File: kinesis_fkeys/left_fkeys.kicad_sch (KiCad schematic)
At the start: 20 parts, among them J2 LEFT_13_TOP, J3 Conn_01x08

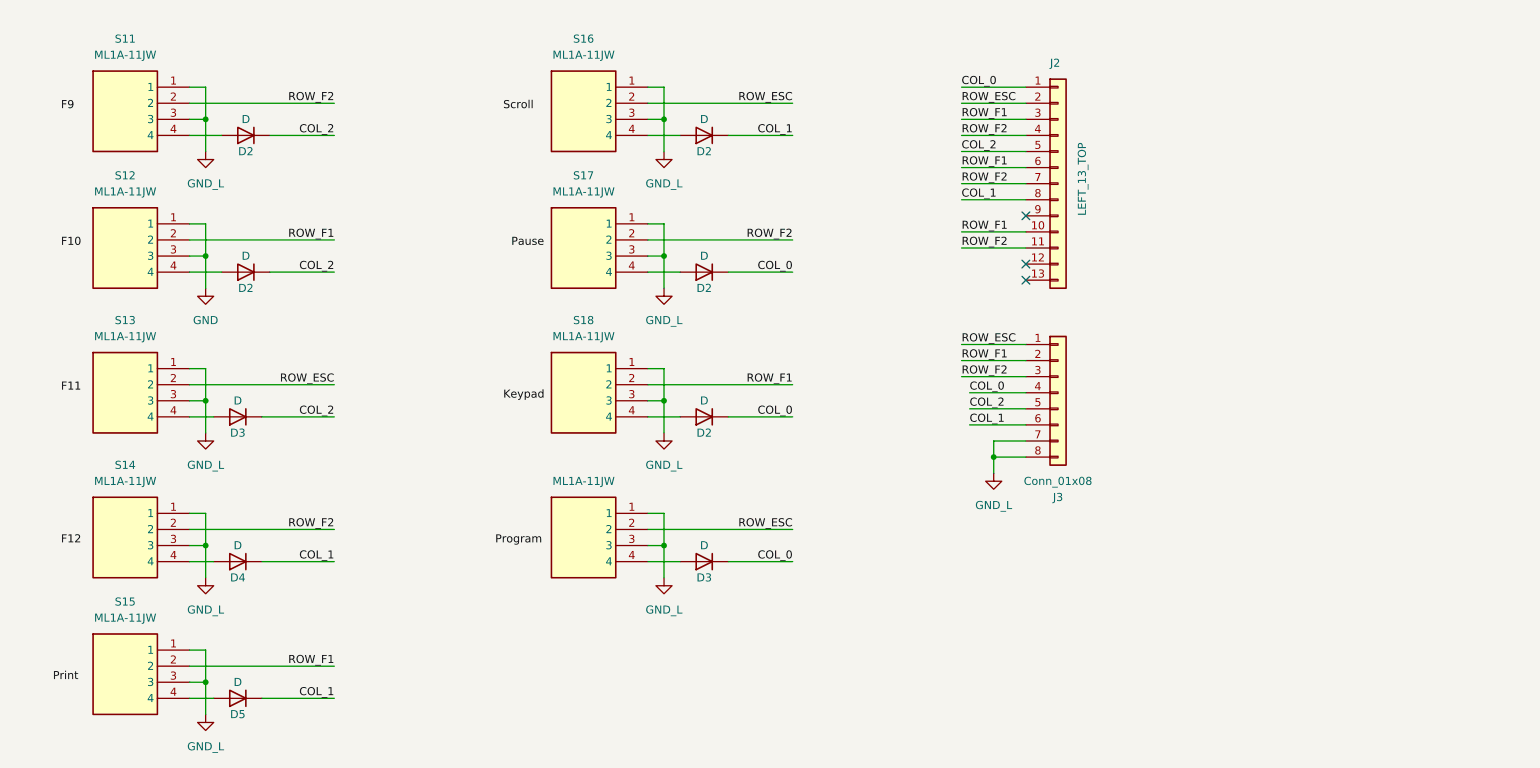
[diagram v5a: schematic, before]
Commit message: created layout - needs to be modified a bit
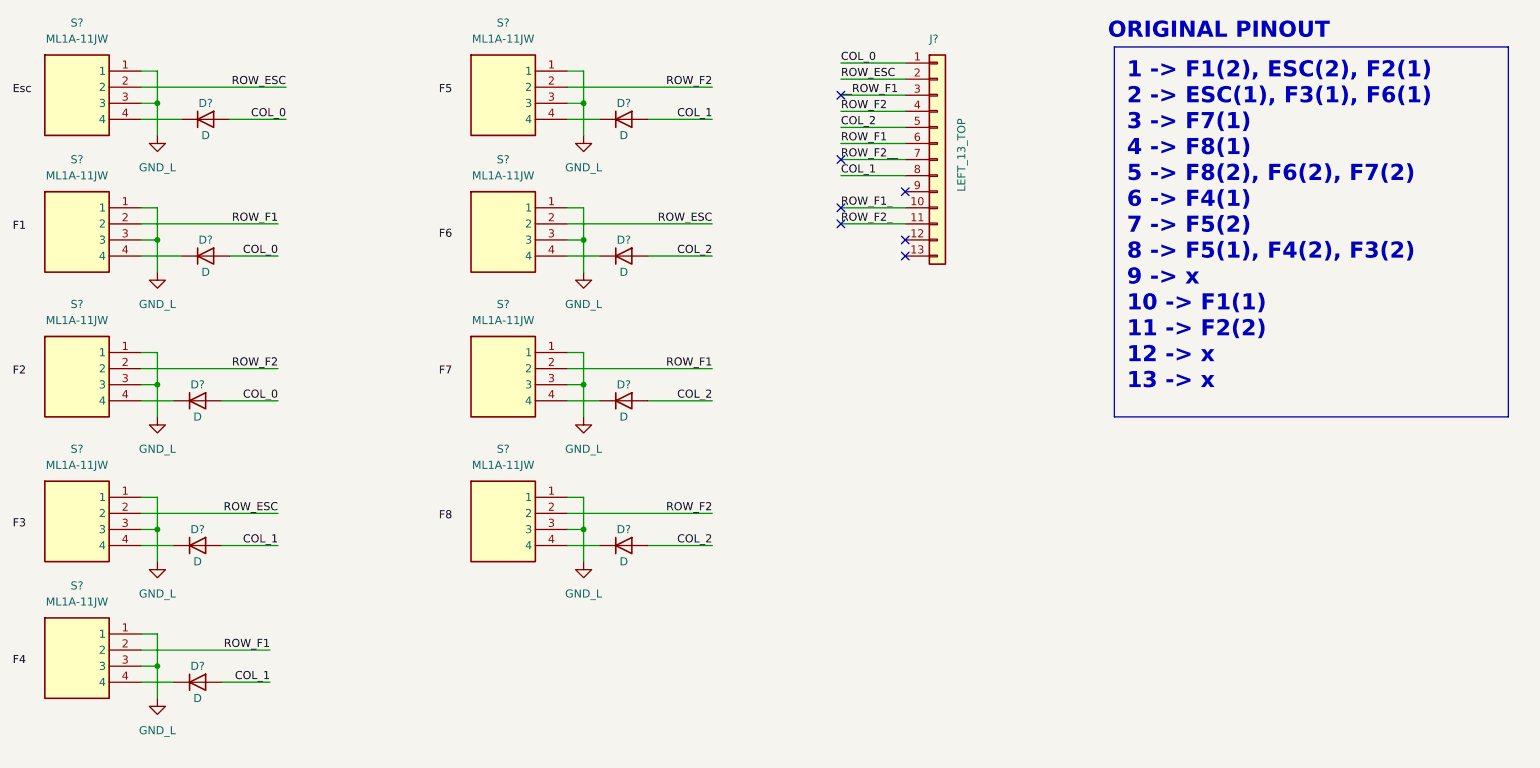
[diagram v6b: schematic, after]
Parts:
- removed D2 (x5), D3 (x2), D4, D5: D, Diode_SMD:D_MiniMELF_Handsoldering, symbol Device:D
- removed J2: LEFT_13_TOP, dodo_conn:Molex-39-53-2135, symbol Connector_Generic:Conn_01x13
- removed J3: Conn_01x08, dodo_conn:84953-6, symbol Connector_Generic:Conn_01x08
- removed S10, S11, S12, S13, S14, S15, S16, S17, S18: ML1A-11JW, dodo_button_and_switch:ML1A11JW, symbol dodo-buttons:ML1A-11JW
- added D? (x9): D, Diode_SMD:D_MiniMELF_Handsoldering, symbol Device:D
- added J?: LEFT_13_TOP, dodo_conn:Molex-39-53-2134, symbol Connector_Generic:Conn_01x13
- added S? (x9): ML1A-11JW, dodo_button_and_switch:ML1A11JW, symbol dodo-buttons:ML1A-11JW
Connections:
- net COL_0: now also D?.2 (A), D?.2 (A), D?.2 (A), J?.1 (Pin_1)
- net COL_1: now also D?.2 (A), D?.2 (A), D?.2 (A), J?.8 (Pin_8)
- net COL_2: now also D?.2 (A), D?.2 (A), D?.2 (A), J?.5 (Pin_5)
- net GND_L: now also S?.1, S?.1, S?.1, S?.1, S?.1, S?.1, S?.1, S?.1, S?.1, S?.3, S?.3, S?.3, S?.3, S?.3, S?.3, S?.3, S?.3, S?.3
- net ROW_ESC: now also J?.2 (Pin_2), S?.2, S?.2, S?.2
- net ROW_F1: now also J?.6 (Pin_6), S?.2, S?.2, S?.2
- net ROW_F2: now also J?.4 (Pin_4), S?.2, S?.2, S?.2
- new net: D?.1 (K), S?.4 (x9)
- new net ROW_F1_: J?.10 (Pin_10)
- new net ROW_F2_: J?.11 (Pin_11)
- new net ROW_F2__: J?.7 (Pin_7)
- new net __ROW_F1: J?.3 (Pin_3)
- no-connect marks 3 -> 7
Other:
- note added: "ORIGINAL PINOUT"

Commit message: removed properties in schematics and updated kicad project version
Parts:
- gave numbers to parts that had none: 19
